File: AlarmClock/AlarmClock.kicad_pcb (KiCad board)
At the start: 2 copper layers, 80 parts, among them J1 PC-GK2.1, J2 Conn_01x04, J3 Conn_01x02, J4 AVR-ISP-6, J5 Conn_01x04, J6 Conn_01x03, J7 Conn_01x03, Q1 BC857, Q10 BCP56, Q11 BCP53, Q12 BC847, Q2 BC857B, Q3 BC847, Q4 IRL6342PbF, Q5 IRL6342PbF, Q6 BC847, Q7 BC847, Q8 BCP56, Q9 BC847, SW1 SW_Push, SW2 SW_Push, SW3 Rotary_Encoder_Switch, SW4 SW_Push, U1 DS3231M, U2 ATmega328P-PU, Y1 16MHz

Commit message: Design the PCB
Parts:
- added C1: 10n, Capacitor_SMD:C_1206_3216Metric_Pad1.33x1.80mm_HandSolder, B.Cu at (162.6, 138.4)
- added D9: 1N4007, Diode_SMD:D_SMA_Handsoldering, B.Cu at (126.3, 83.8)
- added JP3: 0 ohm, Resistor_SMD:R_1206_3216Metric_Pad1.30x1.75mm_HandSolder, B.Cu at (144.8, 87.6)
- added JP4: 0 ohm, Resistor_SMD:R_1206_3216Metric_Pad1.30x1.75mm_HandSolder, B.Cu at (161.3, 105.4)
- added JP5: 0 ohm, Resistor_SMD:R_1206_3216Metric_Pad1.30x1.75mm_HandSolder, B.Cu at (156.8, 132.1)
- added JP6: 0 ohm, Resistor_SMD:R_1206_3216Metric_Pad1.30x1.75mm_HandSolder, B.Cu at (154.9, 101.6)
- added JP7: 0 ohm, Resistor_SMD:R_1206_3216Metric_Pad1.30x1.75mm_HandSolder, B.Cu at (139.7, 121.9)
- added R24: 10k, Resistor_SMD:R_1206_3216Metric_Pad1.30x1.75mm_HandSolder, B.Cu at (179.1, 146.1)
- added R25: 10k, Resistor_SMD:R_1206_3216Metric_Pad1.30x1.75mm_HandSolder, B.Cu at (162.6, 143.5)
- added R26: 10k, Resistor_SMD:R_1206_3216Metric_Pad1.30x1.75mm_HandSolder, B.Cu at (171.4, 138.4)
- added REF**: MountingHole_3.2mm_M3, MountingHole:MountingHole_3.2mm_M3, F.Cu at (186.7, 72.4)
- added REF**: MountingHole_3.2mm_M3, MountingHole:MountingHole_3.2mm_M3, F.Cu at (186.7, 148.6)
- added REF**: MountingHole_3.2mm_M3, MountingHole:MountingHole_3.2mm_M3, F.Cu at (115.6, 148.6)
- added REF**: MountingHole_3.2mm_M3, MountingHole:MountingHole_3.2mm_M3, F.Cu at (115.6, 72.4)
- C10, C11, C12, C13, C3, C4, C6, C9, D1, D2, D5, D7, D8, JP1, JP2, Q1, Q10, Q11, Q12, Q2, Q3, Q4, Q5, Q6, Q7, Q8, Q9, R1, R10, R11, R12, R13, R14, R15, R16, R17, R18, R19, R2, R20, R21, R22, R23, R3, R4, R5, R6, R7, R8, R9, U1: moved to B.Cu
- C17: renamed from C1; moved to B.Cu
- C2: value 100n -> 10n; moved to B.Cu
- C5: value 100n -> 470n; moved to B.Cu
- C7: value 470n -> 100n; moved to B.Cu
- D3, D4: footprint Diode_THT:D_DO-41_SOD81_P10.16mm_Horizontal -> Diode_SMD:D_SMA_Handsoldering; moved to B.Cu
- SW3: footprint Connector_Molex:Molex_KK-254_AE-6410-05A_1x05_P2.54mm_Vertical -> ondra:Rotary_Encode_Switch_Molex_KK-254_AE-6410-05A_1x05_P2.54mm_Vertical
- moved SW3 112.3 mm to (179.1, 142.2), turned to 180 degrees
- moved BT1 111.9 mm to (177.8, 125.7), turned to 90 degrees
- moved JP1 103.4 mm to (177.2, 132.1)
- moved BZ1 100.0 mm to (184.2, 137.2), turned to 90 degrees
- moved J3 98.3 mm to (142.2, 143.5), turned to 180 degrees
- moved D4 91.3 mm to (170.2, 130.8), turned to 270 degrees
- moved R8 91.3 mm to (176.5, 146.1), turned to 90 degrees
- moved L2 86.1 mm to (160.0, 76.2)
- moved C16 83.8 mm to (171.4, 76.2)
- moved R5 82.5 mm to (141.0, 141.2), turned to 180 degrees
- moved D3 82.3 mm to (122.6, 139.7), turned to 90 degrees
- moved U2 82.1 mm to (137.2, 104.1)
- moved R15 80.8 mm to (134.6, 136.5), turned to 90 degrees
- moved J4 79.5 mm to (154.9, 124.5)
- moved R7 79.2 mm to (174.0, 146.1), turned to 90 degrees
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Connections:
- C17 pad 1: /BTN_stop -> /enc_sw
- C2 pad 1: /BTN_snooze -> /enc_clk
- J2 pad 3: GND -> Net-(J2-Pad3)
- J4 pad 4: /MOSI -> Net-(J4-Pad4)
- Q10 pad 1: Net-(Q10-Pad1) -> Net-(JP3-Pad2)
- Q11 pad 1: Net-(Q10-Pad1) -> Net-(JP3-Pad1)
- Q9 pad 3: Net-(Q10-Pad1) -> Net-(JP3-Pad1)
- R23 pad 2: Net-(Q10-Pad1) -> Net-(JP3-Pad2)
- R7 pad 2: /enc_clk -> Net-(R25-Pad1)
- R8 pad 2: /enc_dt -> Net-(R24-Pad1)
- R9 pad 2: /enc_sw -> Net-(R26-Pad2)
- U1 pad 1: (no net) -> Net-(U1-Pad1)
- U1 pad 16: /SCL -> Net-(JP4-Pad2)
- U1 pad 3: (no net) -> Net-(U1-Pad3)
- U1 pad 4: (no net) -> Net-(U1-Pad4)
- U2 pad 14: (no net) -> Net-(U2-Pad14)
- U2 pad 21: (no net) -> Net-(U2-Pad21)
- U2 pad 23: (no net) -> Net-(U2-Pad23)
- U2 pad 24: (no net) -> Net-(U2-Pad24)
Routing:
- net GND: track 0.00 -> 544.0 mm, vias 0 -> 4
- net +5V: track 0.00 -> 420.0 mm, vias 0 -> 12
- net /ambient: track 0.00 -> 105.3 mm
- net /enc_dt: track 0.00 -> 92.6 mm, vias 0 -> 2
- net /audio: track 0.00 -> 80.6 mm, vias 0 -> 2
- net /enc_clk: track 0.00 -> 75.4 mm, vias 0 -> 2
- net Net-(C13-Pad1): track 0.00 -> 59.6 mm
- net /!RST: track 0.00 -> 58.0 mm, vias 0 -> 2
- net /buzzer: track 0.00 -> 53.8 mm
- net /enc_sw: track 0.00 -> 51.3 mm
- net Net-(D7-Pad2): track 0.00 -> 44.5 mm
- net /BTN_stop: track 0.00 -> 35.6 mm
- net Net-(BT1-Pad1): track 0.00 -> 32.6 mm
- net /BTN_snooze: track 0.00 -> 26.0 mm, vias 0 -> 2
- net /SDA: track 0.00 -> 25.8 mm
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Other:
- board outline added: 78.1 x 83.8 mm
- net class Default: clearance 0.2 -> 0.4; trace_width 0.25 -> 1; via_dia 0.8 -> 1; via_drill 0.4 -> 0.8
- rule trace_clearance: 0.2 -> 0.4
- rule trace_min: 0.2 -> 0.8
- rule via_min_drill: 0.3 -> 0.8
- rule via_min_size: 0.4 -> 1

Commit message: Populate I2C pull-up resistors
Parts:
- R3, R4: value DNP -> 3k3

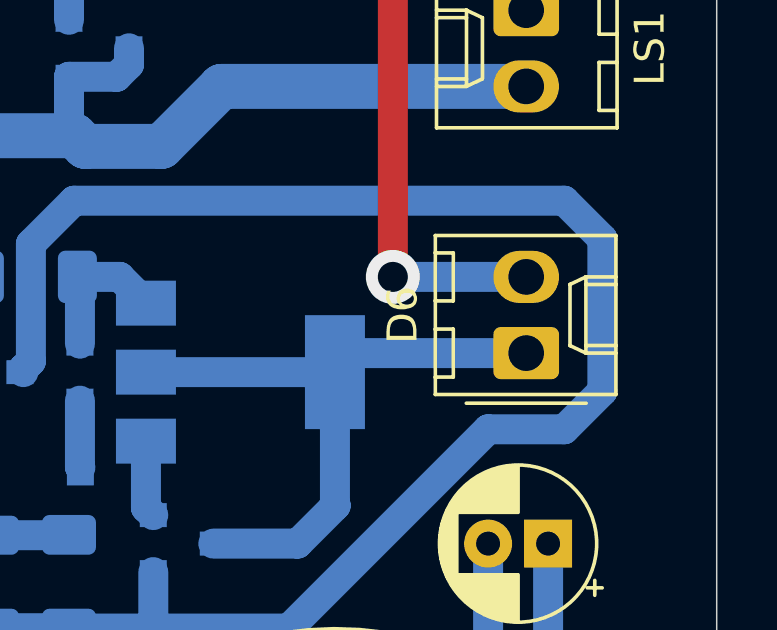
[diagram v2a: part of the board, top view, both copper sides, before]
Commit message: Fix ambient LED staying lit
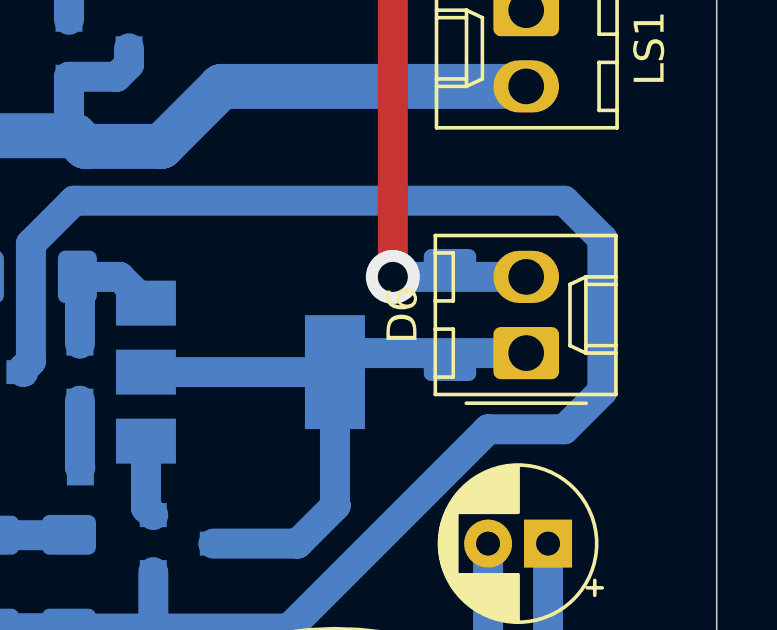
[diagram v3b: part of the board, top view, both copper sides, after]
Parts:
- added R27: 10k, Resistor_SMD:R_1206_3216Metric_Pad1.30x1.75mm_HandSolder, B.Cu at (181.6, 91.4)
